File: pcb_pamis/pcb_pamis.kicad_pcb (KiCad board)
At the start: 2 copper layers, 55 parts, among them J1 USB_C_Receptacle_USB2.0_16P, J10 Conn_01x03, J11 Conn_01x03, J12 Conn_02x06_Odd_Even, J2 1755736, J3 Conn_01x04, J4 Conn_01x04, J5 Conn_01x04, J6 Conn_01x05, J7 Conn_01x05, J8 Conn_01x05, J9 Conn_01x03, Q1 Q_NPN_BEC, Q2 Q_NPN_BEC, SW1 SW_Push, U1 ESP32-WROOM-32UE, U2 CP2102N-Axx-xQFN28, U3 TMC2209_SILENTSTEPSTICK, U4 TMC2209_SILENTSTEPSTICK, U5 TMC2209_SILENTSTEPSTICK

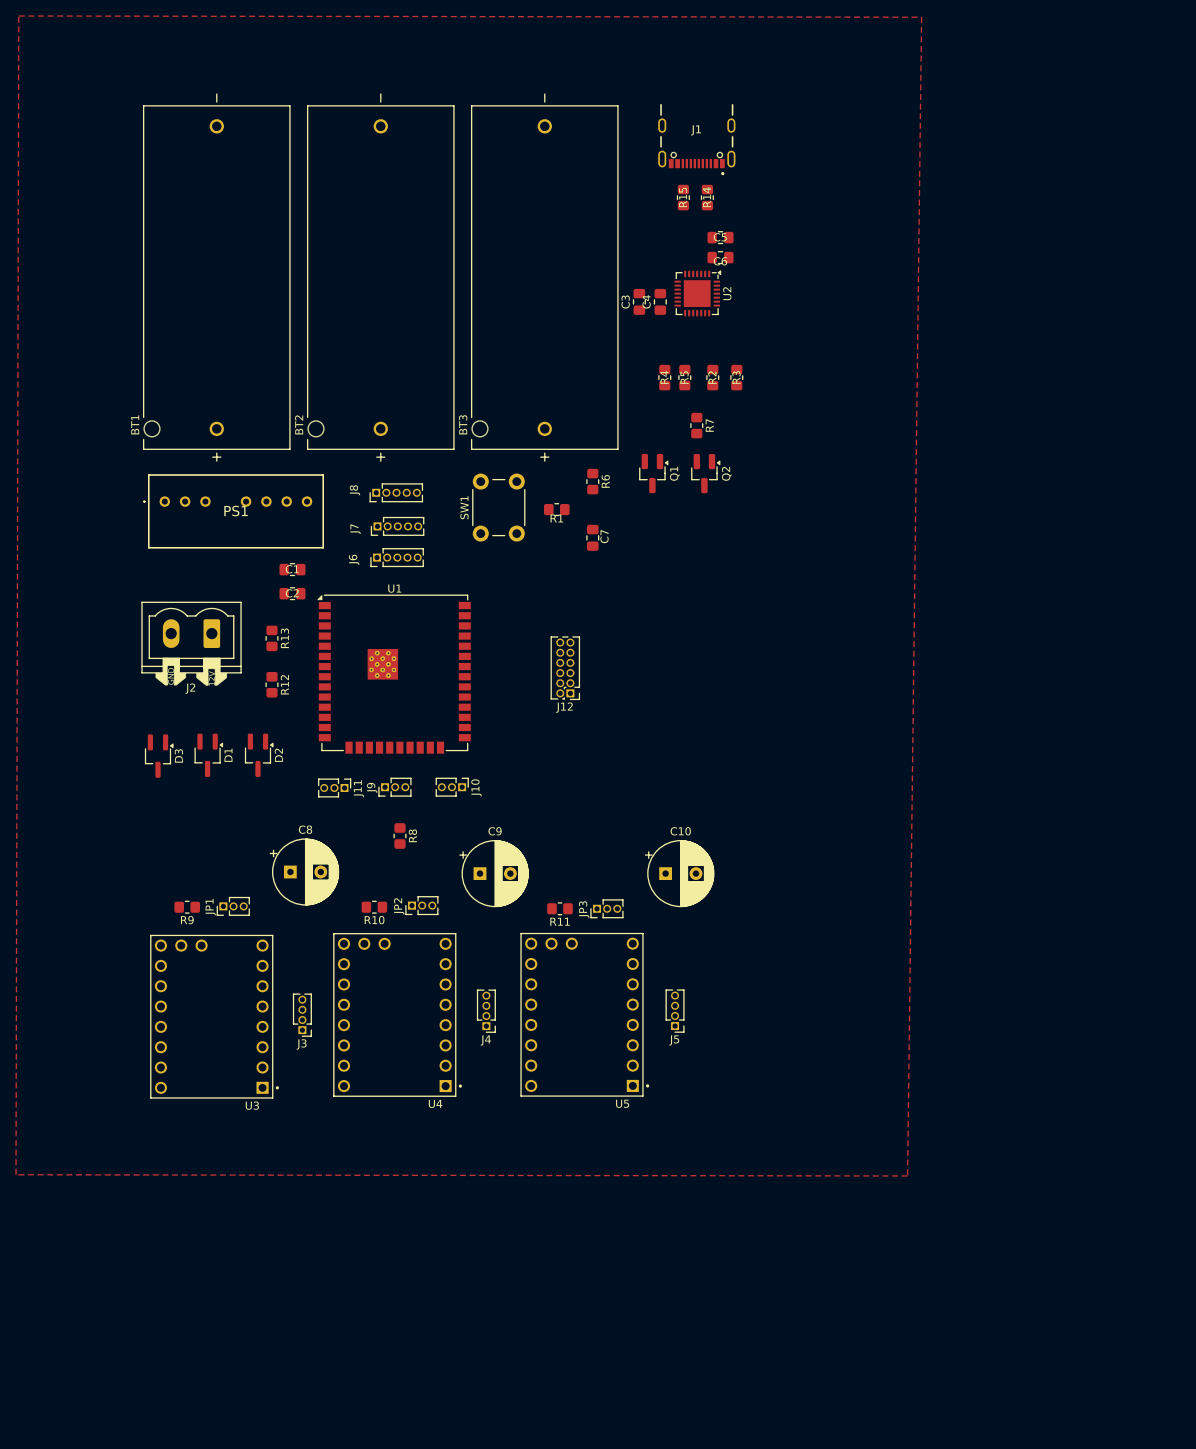
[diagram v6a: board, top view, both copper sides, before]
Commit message: ajustements et optimisations du placement des composants sur PCB Pami
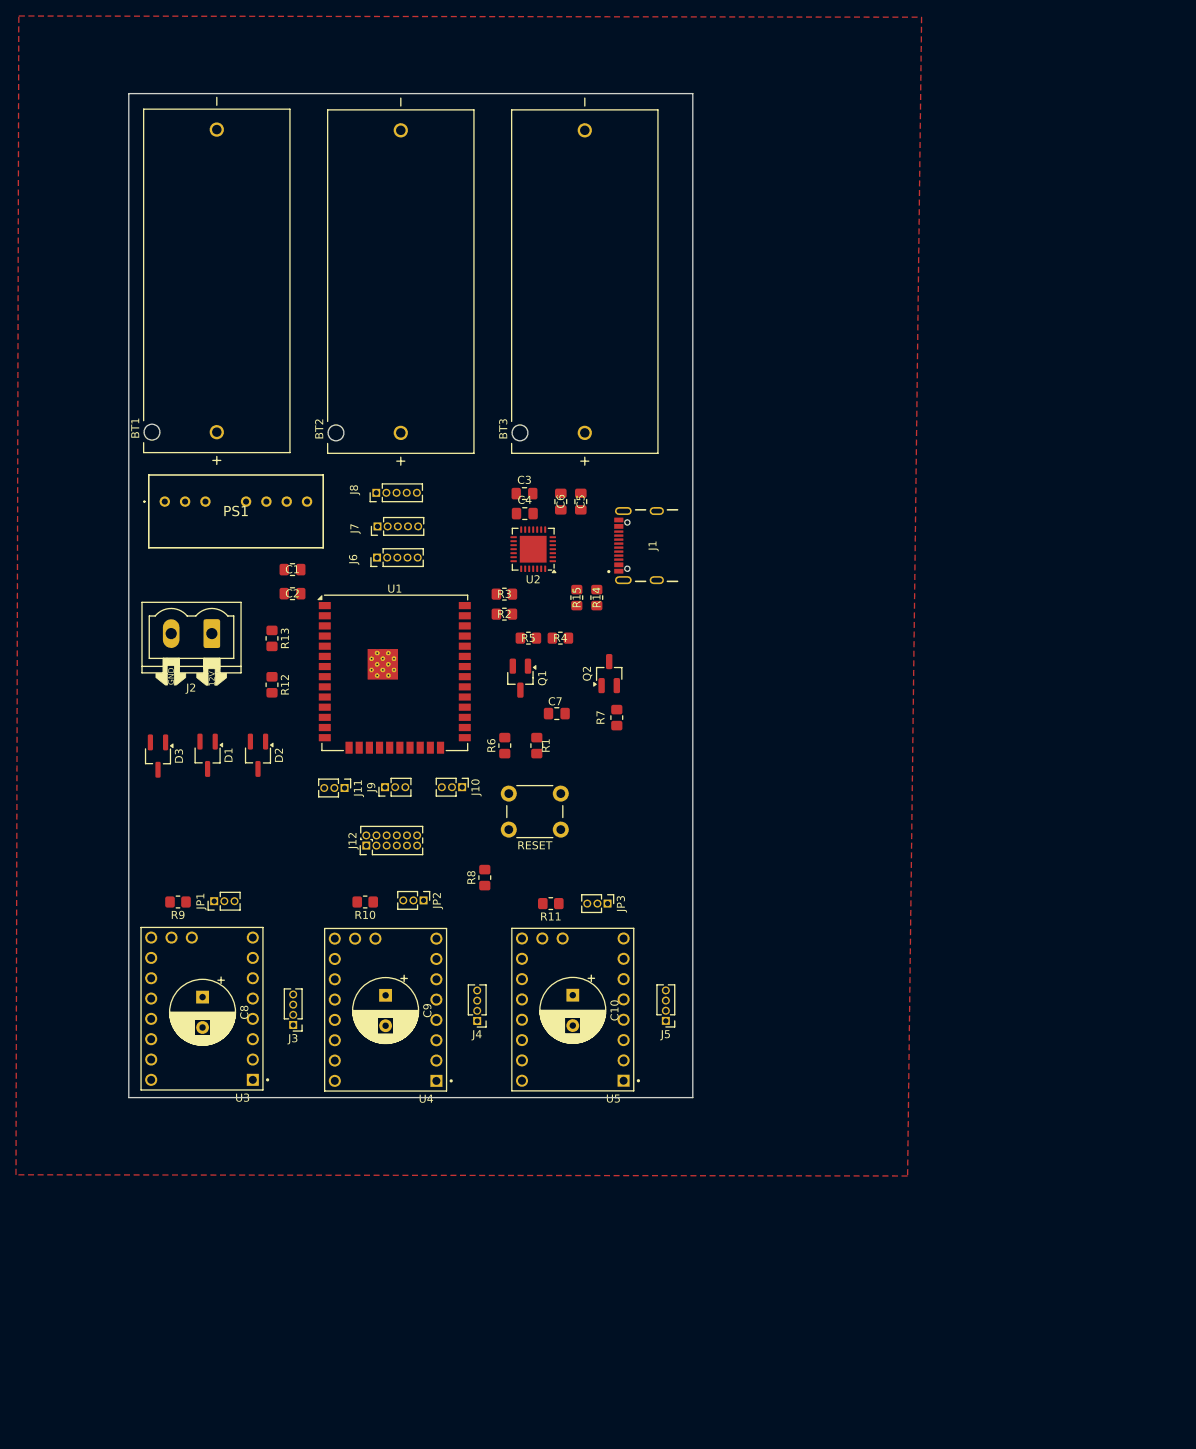
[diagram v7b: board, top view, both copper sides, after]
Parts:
- moved J1 52.7 mm to (141.0, 84.5), turned to 90 degrees
- moved R14 51.9 mm to (133.5, 91.0)
- moved R15 51.7 mm to (131.0, 91.0)
- moved R3 39.7 mm to (122.0, 90.6), turned to 180 degrees
- moved R2 39.4 mm to (122.0, 93.1), turned to 0 degrees
- moved RESET 38.3 mm to (129.0, 120.0), turned to 180 degrees
- moved R5 38.0 mm to (125.0, 96.1), turned to 0 degrees
- moved U2 38.0 mm to (125.5, 85.0), turned to 180 degrees
- moved R7 37.8 mm to (136.0, 106.0), turned to 90 degrees
- moved C5 37.3 mm to (131.5, 79.0), turned to -90 degrees
- moved C6 36.5 mm to (129.0, 79.0), turned to -90 degrees
- moved R4 35.1 mm to (128.9, 96.1), turned to 0 degrees
- moved R6 34.8 mm to (122.0, 109.5), turned to 90 degrees
- moved J12 31.8 mm to (104.7, 122.0), turned to 90 degrees
- moved C4 31.4 mm to (124.5, 80.5), turned to 0 degrees
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- renumbered SW1 to RESET
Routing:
- net EN: track 0.50 -> 0.00 mm
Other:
- board outline added: 70.5 x 125.5 mm

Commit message: miniaturisation PCB Pami
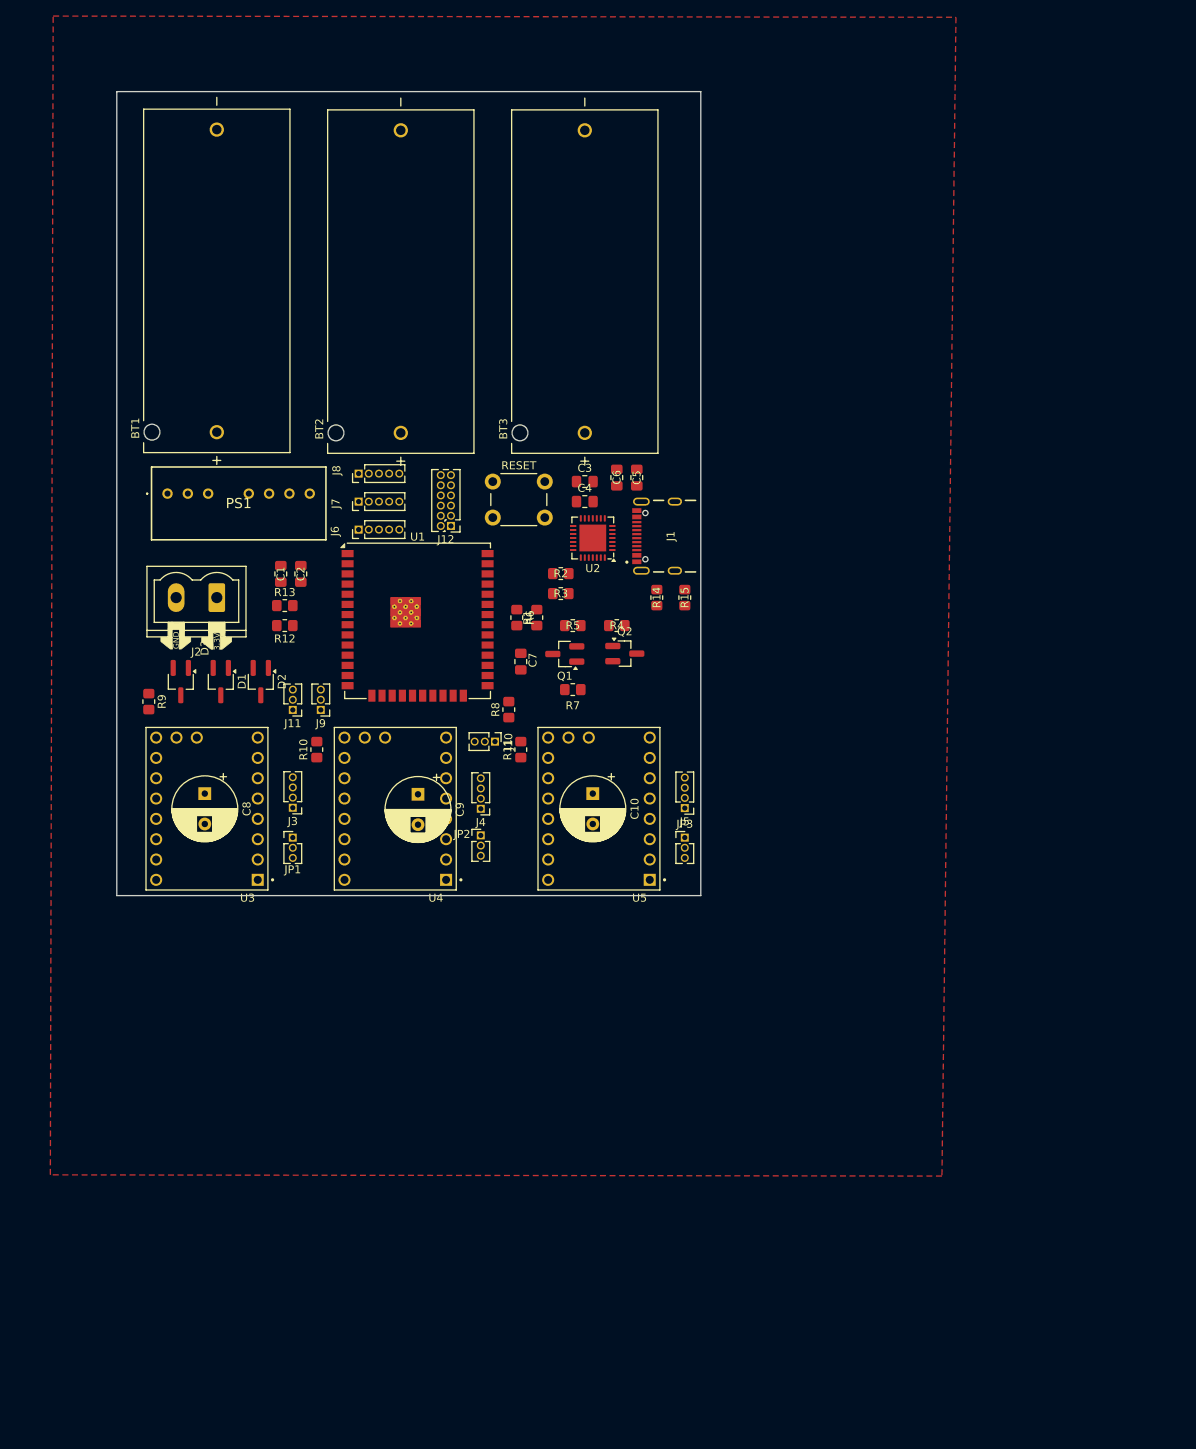
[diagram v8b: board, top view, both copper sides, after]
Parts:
- moved RESET 44.3 mm to (120.5, 76.5), turned to 0 degrees
- moved J12 41.3 mm to (115.3, 82.0), turned to 180 degrees
- moved J3 27.2 mm to (95.5, 117.3)
- moved J5 26.7 mm to (144.5, 117.3)
- moved J4 26.5 mm to (119.0, 117.4)
- moved C9 25.5 mm to (111.2, 115.6)
- moved C8 25.4 mm to (84.5, 115.5)
- moved U5 25.3 mm to (133.8, 117.4)
- moved C10 25.3 mm to (133.0, 115.5)
- moved R9 25.3 mm to (77.5, 104.0), turned to -90 degrees
- moved U4 25.2 mm to (108.3, 117.4)
- moved U3 25.0 mm to (84.8, 117.4)
- moved R8 21.2 mm to (122.5, 105.0)
- moved R10 20.0 mm to (98.5, 110.0), turned to 90 degrees
- moved R11 19.6 mm to (124.0, 110.0), turned to 90 degrees
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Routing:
- net RX_MOTEUR: track 0.53 -> 0.00 mm
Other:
- board size 70.5 x 125.5 mm -> 73 x 100.5 mm
